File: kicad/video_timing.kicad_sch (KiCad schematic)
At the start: 12 parts, among them U13 ATF22V10C-7PX, U14 ATF22V10C-7PX, U15 ATF22V10C-7PX, U29 SN74F541N, U35 ATF22V10C-7PX

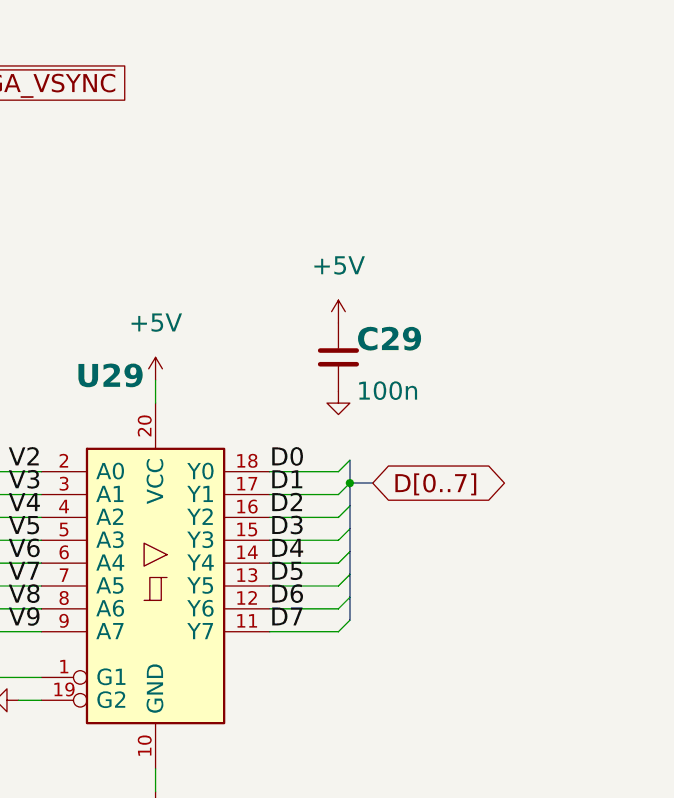
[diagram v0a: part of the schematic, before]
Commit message: Schematic: rename buses to ADDR / DATABUS / D, wire the shared port outputs
- Address bus A15:A0 is now ADDR15:ADDR0, the data bus D7:D0 is DATABUS7:DATABUS0
  and the D register's outputs DR7:DR0 are D7:D0 (main board and both cartridges).
- Shared port sheet: U38's outputs P_SCK, P_MOSI, P_CS, P_PS2D and K0 are wired
  to the SNES pads, the SD dividers and the PS/2 hold diodes (K0 -> D6 ->
  keyboard CLK).  J3 now sits level with U38's SCK/MOSI pins, J2 above it.
- Parts moved so the longer labels fit: U3/U4 and the PC bus, U18, U22, U11,
  U31, U32, RN1, R5-R12; expansion slots in two rows.
- SCHEMATIC_PLAN.md: the bus names.

Co-Authored-By: Claude Opus 5.5 <noreply@anthropic.com>
Claude-Session: https://claude.ai/code/session_01DnW5SUv7E4nz9tGtPvD1qV
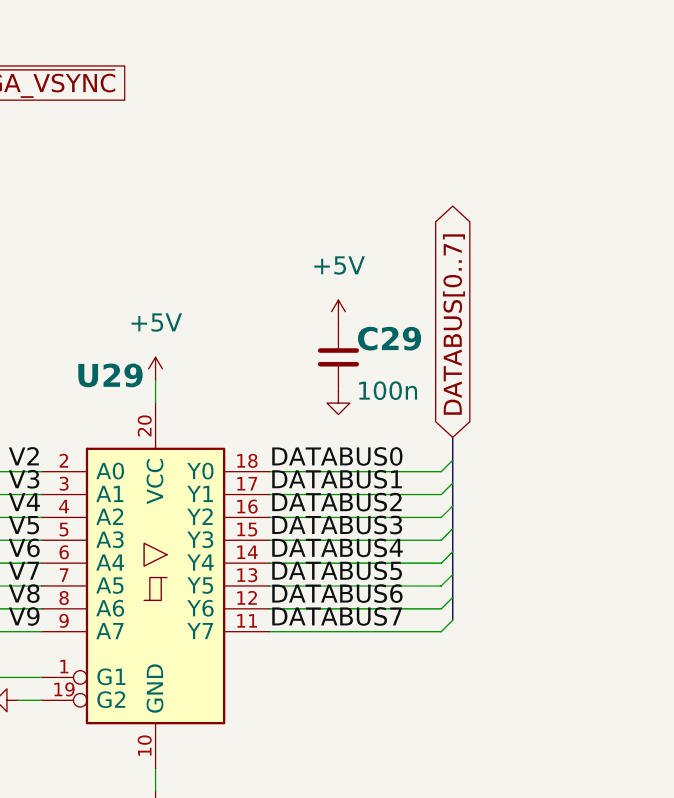
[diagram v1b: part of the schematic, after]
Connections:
- net D0 renamed DATABUS0
- net D1 renamed DATABUS1
- net D2 renamed DATABUS2
- net D3 renamed DATABUS3
- net D4 renamed DATABUS4
- net D5 renamed DATABUS5
- net D6 renamed DATABUS6
- net D7 renamed DATABUS7
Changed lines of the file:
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@@
 (kicad_sch (version 20230121) (generator eeschema)
   (paper "A3")
-  (title_block (title "Placard: Video timing") (date "2026-10-26") (rev "1") (company "Placard computer") (comment 1 "Generated by src/scripts/gen_kicad_schematic.py; plan in docs/SCHEMATIC_PLAN.md") (comment 2 "Chip numbers U1-U42 = docs/CHIPS.md; decoupling Cn goes with Un"))
+  (title_block (title "Placard: Video timing") (date "2026-10-27") (rev "1") (company "Placard computer") (comment 1 "Generated by src/scripts/gen_kicad_schematic.py; plan in docs/SCHEMATIC_PLAN.md") (comment 2 "Chip numbers U1-U42 = docs/CHIPS.md; decoupling Cn goes with Un"))
   (text "Video timing" (at 15 22 0) (effects (font (size 6 6) bold) (justify left bottom)))
   (text "640 x 480 at 60 Hz: H and V counters, Sync, mode and audio slots, line read" (at 15 30 0) (effects (font (size 3 3)) (justify left bottom)))
@@
   (wire (pts (xy 332.74 165.1) (xy 321.31 165.1)) (stroke (width 0) (type default)))
   (global_label "~{LINE_RD}" (shape input) (at 321.31 165.1 180) (fields_autoplaced) (effects (font (size 2 2)) (justify right)) (property "Intersheetrefs" "${INTERSHEET_REFS}" (at 321.31 165.1 0) (effects (font (size 2 2)) (justify left) hide)))
-  (wire (pts (xy 358.14 142.24) (xy 365.76 142.24)) (stroke (width 0) (type default)))
-  (label "D0" (at 358.14 142.24 0) (fields_autoplaced) (effects (font (size 2 2)) (justify left bottom)))
-  (bus_entry (at 365.76 142.24) (size 1.27 -1.27) (stroke (width 0) (type default)))
-  (wire (pts (xy 358.14 144.78) (xy 365.76 144.78)) (stroke (width 0) (type default)))
-  (label "D1" (at 358.14 144.78 0) (fields_autoplaced) (effects (font (size 2 2)) (justify left bottom)))
-  (bus_entry (at 365.76 144.78) (size 1.27 -1.27) (stroke (width 0) (type default)))
-  (wire (pts (xy 358.14 147.32) (xy 365.76 147.32)) (stroke (width 0) (type default)))
-  (label "D2" (at 358.14 147.32 0) (fields_autoplaced) (effects (font (size 2 2)) (justify left bottom)))
-  (bus_entry (at 365.76 147.32) (size 1.27 -1.27) (stroke (width 0) (type default)))
-  (wire (pts (xy 358.14 149.86) (xy 365.76 149.86)) (stroke (width 0) (type default)))
-  (label "D3" (at 358.14 149.86 0) (fields_autoplaced) (effects (font (size 2 2)) (justify left bottom)))
-  (bus_entry (at 365.76 149.86) (size 1.27 -1.27) (stroke (width 0) (type default)))
-  (wire (pts (xy 358.14 152.4) (xy 365.76 152.4)) (stroke (width 0) (type default)))
-  (label "D4" (at 358.14 152.4 0) (fields_autoplaced) (effects (font (size 2 2)) (justify left bottom)))
-  (bus_entry (at 365.76 152.4) (size 1.27 -1.27) (stroke (width 0) (type default)))
-  (wire (pts (xy 358.14 154.94) (xy 365.76 154.94)) (stroke (width 0) (type default)))
-  (label "D5" (at 358.14 154.94 0) (fields_autoplaced) (effects (font (size 2 2)) (justify left bottom)))
-  (bus_entry (at 365.76 154.94) (size 1.27 -1.27) (stroke (width 0) (type default)))
-  (wire (pts (xy 358.14 157.48) (xy 365.76 157.48)) (stroke (width 0) (type default)))
-  (label "D6" (at 358.14 157.48 0) (fields_autoplaced) (effects (font (size 2 2)) (justify left bottom)))
-  (bus_entry (at 365.76 157.48) (size 1.27 -1.27) (stroke (width 0) (type default)))
-  (wire (pts (xy 358.14 160.02) (xy 365.76 160.02)) (stroke (width 0) (type default)))
-  (label "D7" (at 358.14 160.02 0) (fields_autoplaced) (effects (font (size 2 2)) (justify left bottom)))
-  (bus_entry (at 365.76 160.02) (size 1.27 -1.27) (stroke (width 0) (type default)))
-  (bus (pts (xy 367.03 140.97) (xy 367.03 143.51)) (stroke (width 0) (type default)))
-  (bus (pts (xy 367.03 143.51) (xy 367.03 146.05)) (stroke (width 0) (type default)))
-  (bus (pts (xy 367.03 146.05) (xy 367.03 148.59)) (stroke (width 0) (type default)))
-  (bus (pts (xy 367.03 148.59) (xy 367.03 151.13)) (stroke (width 0) (type default)))
-  (bus (pts (xy 367.03 151.13) (xy 367.03 153.67)) (stroke (width 0) (type default)))
-  (bus (pts (xy 367.03 153.67) (xy 367.03 156.21)) (stroke (width 0) (type default)))
-  (bus (pts (xy 367.03 156.21) (xy 367.03 158.75)) (stroke (width 0) (type default)))
+  (wire (pts (xy 358.14 142.24) (xy 377.19 142.24)) (stroke (width 0) (type default)))
+  (label "DATABUS0" (at 358.14 142.24 0) (fields_autoplaced) (effects (font (size 2 2)) (justify left bottom)))
+  (bus_entry (at 377.19 142.24) (size 1.27 -1.27) (stroke (width 0) (type default)))
+  (wire (pts (xy 358.14 144.78) (xy 377.19 144.78)) (stroke (width 0) (type default)))
+  (label "DATABUS1" (at 358.14 144.78 0) (fields_autoplaced) (effects (font (size 2 2)) (justify left bottom)))
+  (bus_entry (at 377.19 144.78) (size 1.27 -1.27) (stroke (width 0) (type default)))
+  (wire (pts (xy 358.14 147.32) (xy 377.19 147.32)) (stroke (width 0) (type default)))
+  (label "DATABUS2" (at 358.14 147.32 0) (fields_autoplaced) (effects (font (size 2 2)) (justify left bottom)))
+  (bus_entry (at 377.19 147.32) (size 1.27 -1.27) (stroke (width 0) (type default)))
+  (wire (pts (xy 358.14 149.86) (xy 377.19 149.86)) (stroke (width 0) (type default)))
+  (label "DATABUS3" (at 358.14 149.86 0) (fields_autoplaced) (effects (font (size 2 2)) (justify left bottom)))
+  (bus_entry (at 377.19 149.86) (size 1.27 -1.27) (stroke (width 0) (type default)))
+  (wire (pts (xy 358.14 152.4) (xy 377.19 152.4)) (stroke (width 0) (type default)))
+  (label "DATABUS4" (at 358.14 152.4 0) (fields_autoplaced) (effects (font (size 2 2)) (justify left bottom)))
+  (bus_entry (at 377.19 152.4) (size 1.27 -1.27) (stroke (width 0) (type default)))
+  (wire (pts (xy 358.14 154.94) (xy 377.19 154.94)) (stroke (width 0) (type default)))
+  (label "DATABUS5" (at 358.14 154.94 0) (fields_autoplaced) (effects (font (size 2 2)) (justify left bottom)))
+  (bus_entry (at 377.19 154.94) (size 1.27 -1.27) (stroke (width 0) (type default)))
+  (wire (pts (xy 358.14 157.48) (xy 377.19 157.48)) (stroke (width 0) (type default)))
+  (label "DATABUS6" (at 358.14 157.48 0) (fields_autoplaced) (effects (font (size 2 2)) (justify left bottom)))
+  (bus_entry (at 377.19 157.48) (size 1.27 -1.27) (stroke (width 0) (type default)))
+  (wire (pts (xy 358.14 160.02) (xy 377.19 160.02)) (stroke (width 0) (type default)))
+  (label "DATABUS7" (at 358.14 160.02 0) (fields_autoplaced) (effects (font (size 2 2)) (justify left bottom)))
+  (bus_entry (at 377.19 160.02) (size 1.27 -1.27) (stroke (width 0) (type default)))
+  (bus (pts (xy 378.46 140.97) (xy 378.46 143.51)) (stroke (width 0) (type default)))
+  (bus (pts (xy 378.46 143.51) (xy 378.46 146.05)) (stroke (width 0) (type default)))
+  (bus (pts (xy 378.46 146.05) (xy 378.46 148.59)) (stroke (width 0) (type default)))
+  (bus (pts (xy 378.46 148.59) (xy 378.46 151.13)) (stroke (width 0) (type default)))
+  (bus (pts (xy 378.46 151.13) (xy 378.46 153.67)) (stroke (width 0) (type default)))
+  (bus (pts (xy 378.46 153.67) (xy 378.46 156.21)) (stroke (width 0) (type default)))
+  (bus (pts (xy 378.46 156.21) (xy 378.46 158.75)) (stroke (width 0) (type default)))
   (global_label "~{VGA_HSYNC}" (shape passive) (at 130.81 96.52 0) (fields_autoplaced) (effects (font (size 2 2)) (justify left)) (property "Intersheetrefs" "${INTERSHEET_REFS}" (at 130.81 96.52 0) (effects (font (size 2 2)) (justify left) hide)))
   (global_label "~{VGA_VSYNC}" (shape passive) (at 323.85 99.06 0) (fields_autoplaced) (effects (font (size 2 2)) (justify left)) (property "Intersheetrefs" "${INTERSHEET_REFS}" (at 323.85 99.06 0) (effects (font (size 2 2)) (justify left) hide)))
@@
   (junction (at 261.62 184.15) (diameter 0) (color 0 0 0 0))
   (global_label "VA[0..8]" (shape bidirectional) (at 264.16 184.15 0) (fields_autoplaced) (effects (font (size 2 2)) (justify left)) (property "Intersheetrefs" "${INTERSHEET_REFS}" (at 264.16 184.15 0) (effects (font (size 2 2)) (justify left) hide)))
-  (bus (pts (xy 367.03 143.51) (xy 369.57 143.51)) (stroke (width 0) (type default)))
-  (junction (at 367.03 143.51) (diameter 0) (color 0 0 0 0))
-  (global_label "D[0..7]" (shape bidirectional) (at 369.57 143.51 0) (fields_autoplaced) (effects (font (size 2 2)) (justify left)) (property "Intersheetrefs" "${INTERSHEET_REFS}" (at 369.57 143.51 0) (effects (font (size 2 2)) (justify left) hide)))
+  (bus (pts (xy 378.46 140.97) (xy 378.46 138.43)) (stroke (width 0) (type default)))
+  (global_label "DATABUS[0..7]" (shape bidirectional) (at 378.46 138.43 90) (fields_autoplaced) (effects (font (size 2 2)) (justify left)) (property "Intersheetrefs" "${INTERSHEET_REFS}" (at 378.46 138.43 0) (effects (font (size 2 2)) (justify left) hide)))
   (wire (pts (xy 200.66 83.82) (xy 109.22 83.82)) (stroke (width 0) (type default)))
   (wire (pts (xy 109.22 83.82) (xy 109.22 101.6)) (stroke (width 0) (type default)))

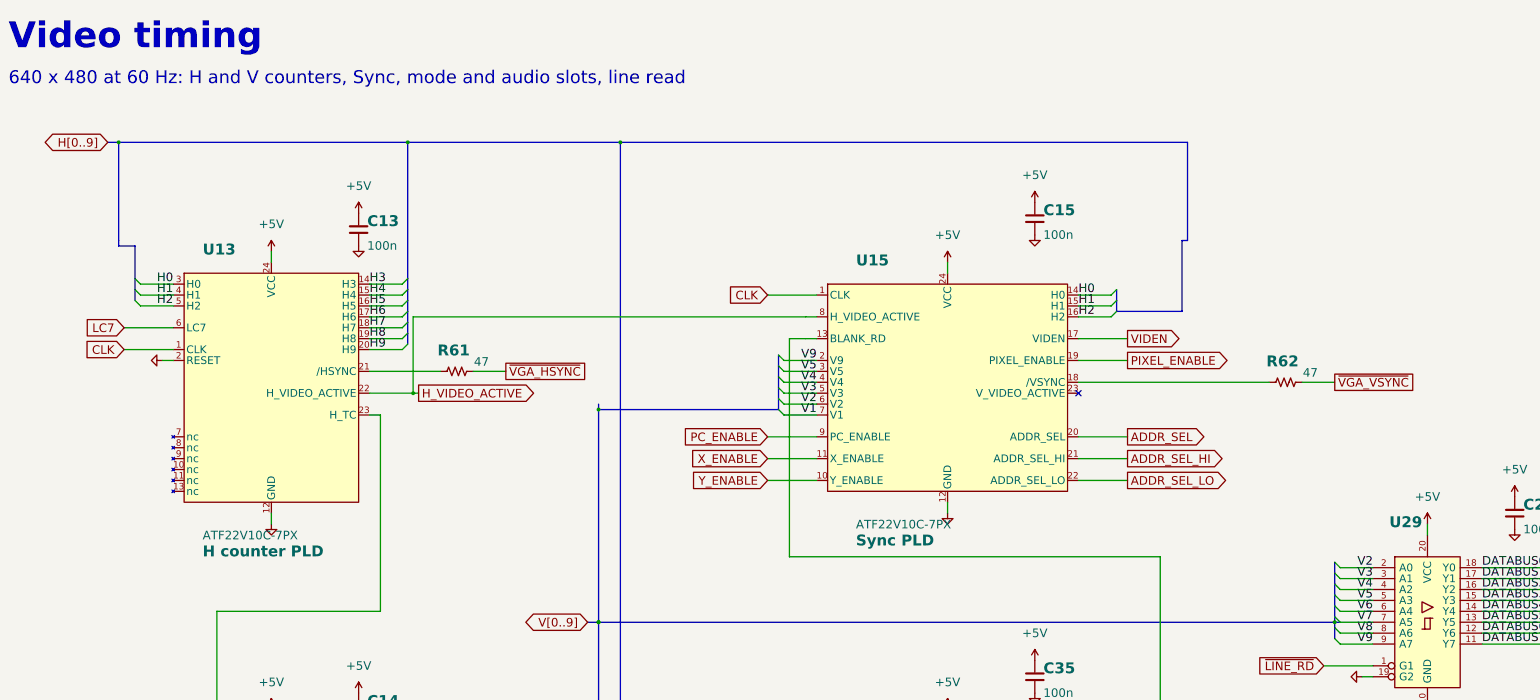
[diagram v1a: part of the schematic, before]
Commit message: Option B: muxes take the enables as selects, /WE from an early clock tap
Removes the Sync PLD pass from every memory address (docs/FETCH_TIMING.md):
the instruction fetch gains 8.2 ns, X/Y/video/upper-32K reads 9.7 ns, the
zero-page store start 6.9 ns, and the address hold after /WE is +0.5 ns
from the datasheets alone.  No new parts, no extra clock, no PLCC.

- ATF22V10_QUAD_MUX.pld rev 02: two low + two high address bits per chip,
  PIXEL_ENABLE / PC_ENABLE / X_ENABLE / Y_ENABLE as the selects
- ATF22V10_SYNC.pld rev 10: ADDR_SEL outputs gone; /WE on pin 20 from the
  early clock tap CLK_E (pin 9), RW and RUN inputs, OE = RUN
- ATF22V10_MEM_CTRL.pld rev 10: /WE gone (pin 16 free)
- ATF22V10_IO_DECODE.pld rev 05: /CE_HI from the enables, RW dropped
- FPGA model and benches follow; GHDL: tb_cart_load (2 seeds), tb_top_load,
  tb_blank_line pass, and cpu_test makes the same 69,776 RAM writes as main
- Schematic: mux sheet rewired, /WE from U15, net tie NT2 between CLK_E and
  CLK on the power sheet (the 500 mm of track), symbols regenerated, PDFs
- Docs updated; docs/option_b_board.png shows the board rewiring (no chip
  has to move)

Co-Authored-By: Claude Fable 5.1 <noreply@anthropic.com>
Claude-Session: https://claude.ai/code/session_01DnW5SSBUc8XDbr4GrYdwj8
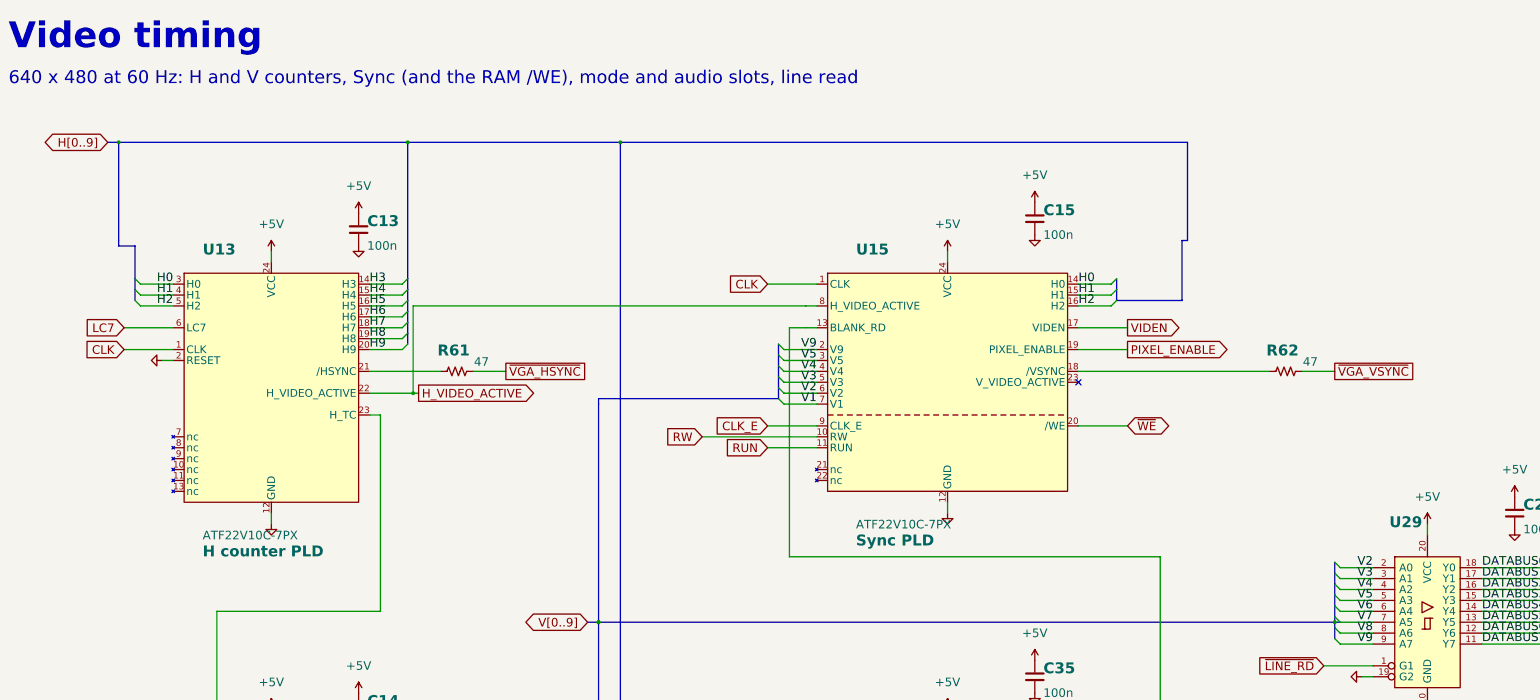
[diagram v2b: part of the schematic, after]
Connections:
- net ADDR_SEL renamed ~{WE}
- net ADDR_SEL_HI: no longer names the net of U15.21 (nc)
- net ADDR_SEL_LO: no longer names the net of U15.22 (nc)
- net PC_ENABLE renamed CLK_E
- net X_ENABLE renamed RUN
- net Y_ENABLE renamed RW
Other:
- note added: "640 x 480 at 60 Hz: H and V counters, Sync (and the RAM /WE), mode and audio slots, line read"
- note removed: "640 x 480 at 60 Hz: H and V counters, Sync, mode and audio slots, line read"
- moved on the sheet: R62
